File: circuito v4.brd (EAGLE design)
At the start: 93.5 x 59.5 mm, 64 parts, among them IC1 LM324N

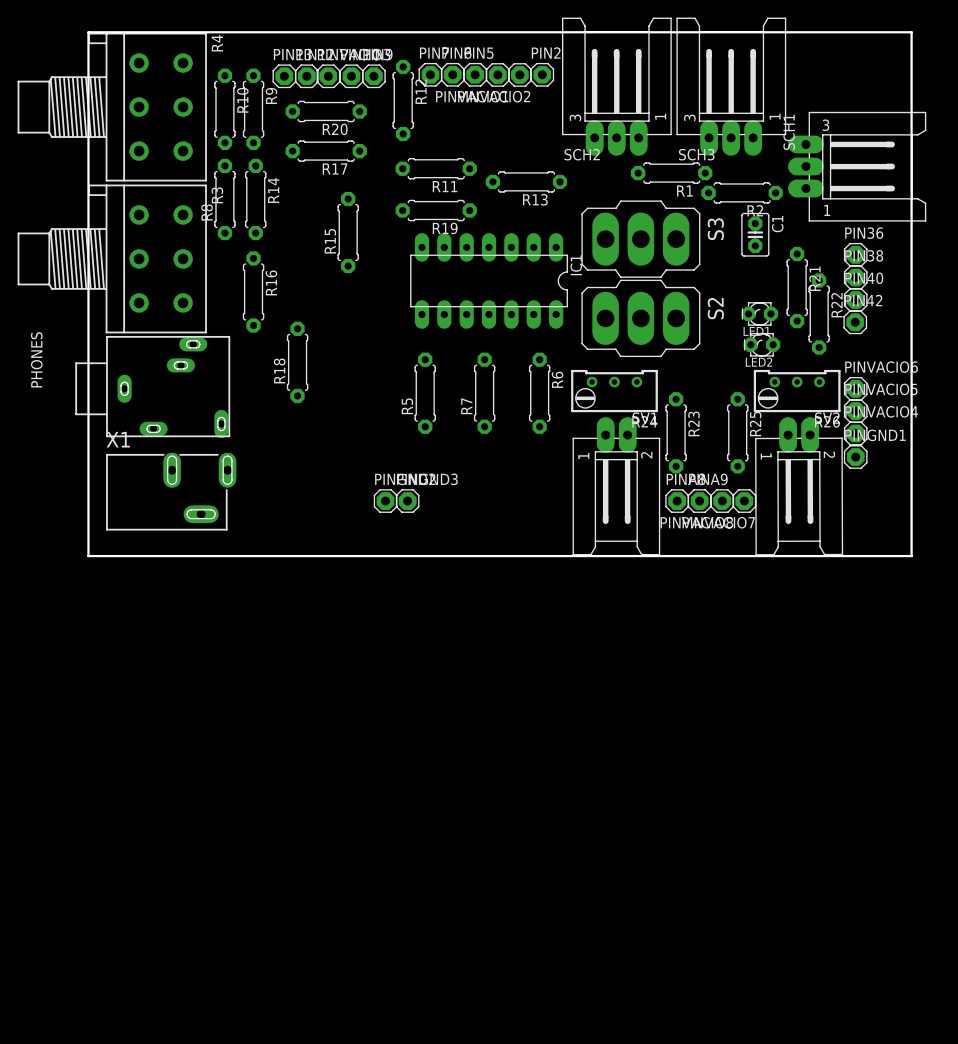
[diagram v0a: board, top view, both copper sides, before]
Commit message: board y sch con elemento ICSP del arduino incluido
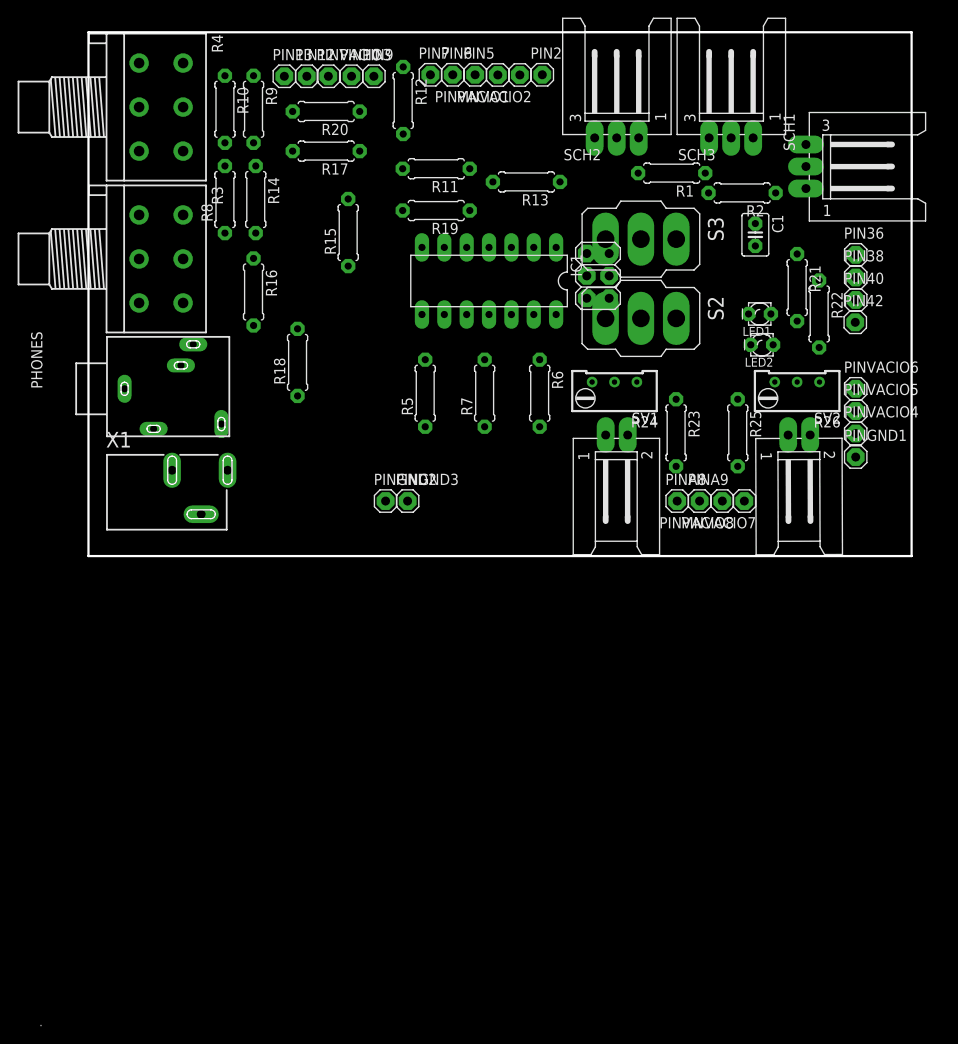
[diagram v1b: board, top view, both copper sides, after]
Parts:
- added JP19: (no value), pinhead:2X03
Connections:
- new net 5V_2: JP19.2
- new net CLK: JP19.3
- new net MISO: JP19.1
- new net MOSI: JP19.4
- new net RESET_2: JP19.5
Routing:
- added copper zone on layer 16, net N$10
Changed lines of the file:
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@@
 <grid distance="0.25" unitdist="mm" unit="mm" style="lines" multiple="1" display="yes" altdistance="0.025" altunitdist="inch" altunit="inch"/>
 <layers>
-<layer number="1" name="Top" color="4" fill="1" visible="yes" active="yes"/>
+<layer number="1" name="Top" color="4" fill="1" visible="no" active="yes"/>
 <layer number="2" name="Route2" color="1" fill="3" visible="no" active="no"/>
 <layer number="3" name="Route3" color="4" fill="3" visible="no" active="no"/>
@@
 <layer number="14" name="Route14" color="1" fill="6" visible="no" active="no"/>
 <layer number="15" name="Route15" color="4" fill="6" visible="no" active="no"/>
-<layer number="16" name="Bottom" color="1" fill="1" visible="yes" active="yes"/>
-<layer number="17" name="Pads" color="2" fill="1" visible="yes" active="yes"/>
-<layer number="18" name="Vias" color="2" fill="1" visible="yes" active="yes"/>
+<layer number="16" name="Bottom" color="1" fill="1" visible="no" active="yes"/>
+<layer number="17" name="Pads" color="2" fill="1" visible="no" active="yes"/>
+<layer number="18" name="Vias" color="2" fill="1" visible="no" active="yes"/>
 <layer number="19" name="Unrouted" color="6" fill="1" visible="yes" active="yes"/>
 <layer number="20" name="Dimension" color="15" fill="1" visible="yes" active="yes"/>
@@
 <layer number="39" name="tKeepout" color="4" fill="11" visible="yes" active="yes"/>
 <layer number="40" name="bKeepout" color="1" fill="11" visible="yes" active="yes"/>
-<layer number="41" name="tRestrict" color="4" fill="10" visible="yes" active="yes"/>
-<layer number="42" name="bRestrict" color="1" fill="10" visible="yes" active="yes"/>
+<layer number="41" name="tRestrict" color="4" fill="10" visible="no" active="yes"/>
+<layer number="42" name="bRestrict" color="1" fill="10" visible="no" active="yes"/>
 <layer number="43" name="vRestrict" color="2" fill="10" visible="no" active="yes"/>
 <layer number="44" name="Drills" color="7" fill="1" visible="no" active="yes"/>
@@
 <attribute name="VALUE" x="59.975" y="34.79" size="1.778" layer="27" ratio="10" rot="R270"/>
 </element>
+<element name="JP19" library="pinhead" package="2X03" value="" x="64.625796875" y="28.07624375" smashed="yes" rot="R90">
+<attribute name="VALUE" x="69.070796875" y="24.26624375" size="1.27" layer="27" rot="R90"/>
+</element>
 </elements>
 <signals>
@@
 <wire x1="80.5" y1="14.06" x2="84.71" y2="16.02" width="0" layer="19" extent="1-1"/>
 </signal>
+<signal name="MOSI">
+<contactref element="JP19" pad="4"/>
+</signal>
+<signal name="MISO">
+<contactref element="JP19" pad="1"/>
+</signal>
+<signal name="CLK">
+<contactref element="JP19" pad="3"/>
+</signal>
+<signal name="N$10">
+<polygon width="0" layer="16">
+<vertex x="1.353546875" y="-57.15"/>
+<vertex x="1.353546875" y="-57.004240625"/>
+<vertex x="1.3581" y="-57.004240625"/>
+</polygon>
+</signal>
+<signal name="RESET_2">
+<contactref element="JP19" pad="5"/>
+</signal>
+<signal name="5V_2">
+<contactref element="JP19" pad="2"/>
+</signal>
 </signals>

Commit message: Poligono bRestrict en ICSP
Se agregó polígono en bRestrict en ICSP.
Se corrieron elementos para que entre ese polígono.
No se agrandó la placa del lado derecho.
Se achicó del lado izquierdo para que la distancia entre el borde de la placa y el centro del pin GND sea 27mm.
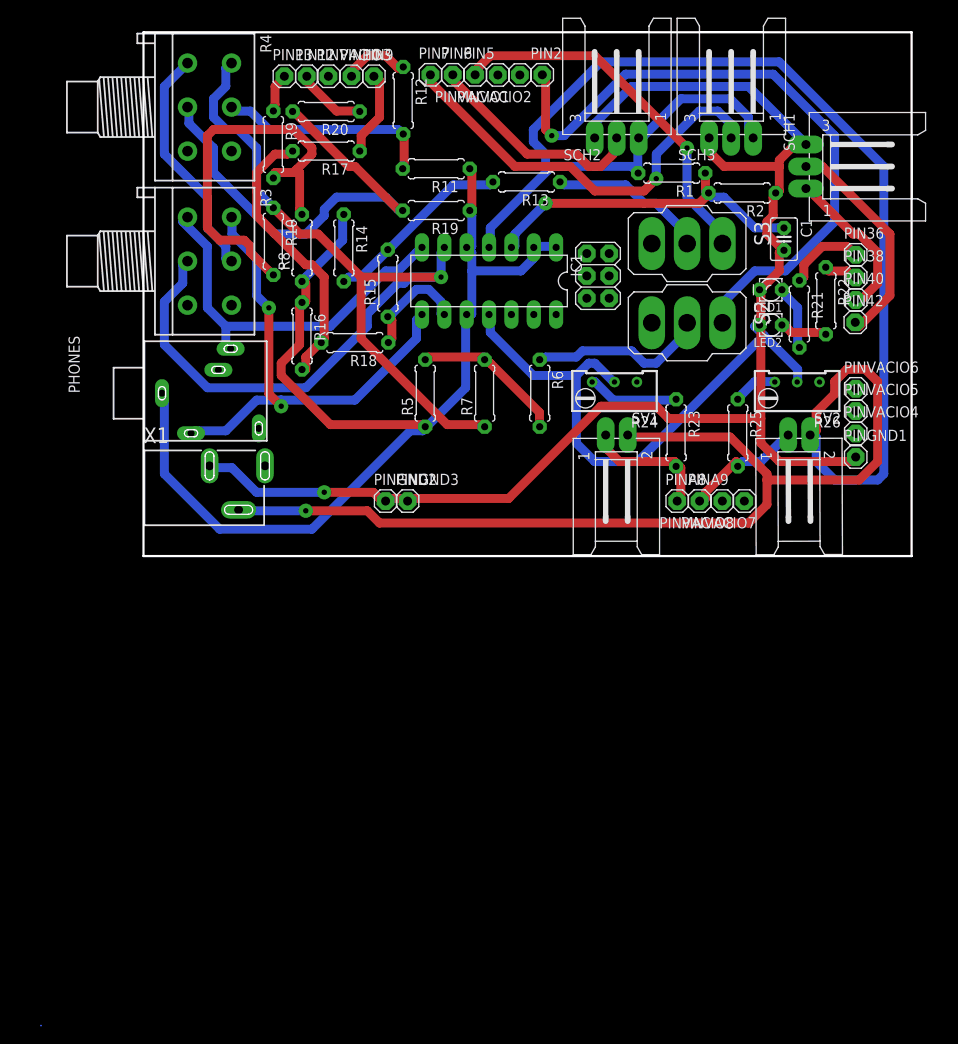
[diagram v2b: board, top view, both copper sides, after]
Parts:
- moved R10 16.0 mm to (27.8, 32.0)
- moved R14 11.4 mm to (35.8, 31.2)
- moved R8 10.3 mm to (31.0, 31.2)
- moved R16 7.43 mm to (31.0, 21.2)
- moved R15 7.30 mm to (40.8, 27.2)
- moved R18 6.88 mm to (37.0, 20.5), turned to 180 degrees
- moved R3 5.51 mm to (18.0, 29.8)
- moved R4 5.50 mm to (18.0, 47.2)
- moved S2 5.27 mm to (74.8, 22.8)
- moved S3 5.27 mm to (74.8, 31.8)
- moved R9 4.59 mm to (27.8, 43.0)
- moved PHONES 4.28 mm to (13.0, 14.8)
- moved X1 4.28 mm to (13.0, 4.00)
- moved C1 3.29 mm to (85.8, 32.2)
- moved LED1 3.02 mm to (84.2, 26.5)
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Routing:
- net VCC: track 0.00 -> 263.0 mm, vias 0 -> 1
- net GND: track 0.00 -> 225.1 mm, vias 0 -> 1
- net N$8: track 0.00 -> 131.2 mm
- net N$4: track 0.00 -> 122.1 mm, vias 0 -> 1
- net N$7: track 0.00 -> 73.8 mm, vias 0 -> 1
- net N$30: track 0.00 -> 57.5 mm, vias 0 -> 2
- net N$18: track 0.00 -> 52.9 mm
- net N$28: track 0.00 -> 47.7 mm, vias 0 -> 1
- net N$9: track 0.00 -> 45.3 mm
- net N$37: track 0.00 -> 43.4 mm
- net N$16: track 0.00 -> 42.3 mm, vias 0 -> 1
- net N$13: track 0.00 -> 39.9 mm
- net N$1: track 0.00 -> 38.5 mm, vias 0 -> 1
- net N$19: track 0.00 -> 32.3 mm
- net N$29: track 0.00 -> 25.4 mm
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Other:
- board size 93.5 x 59.5 mm -> 87.2 x 59.5 mm

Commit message: Agrego vRestrict en OpAmp y Switchs
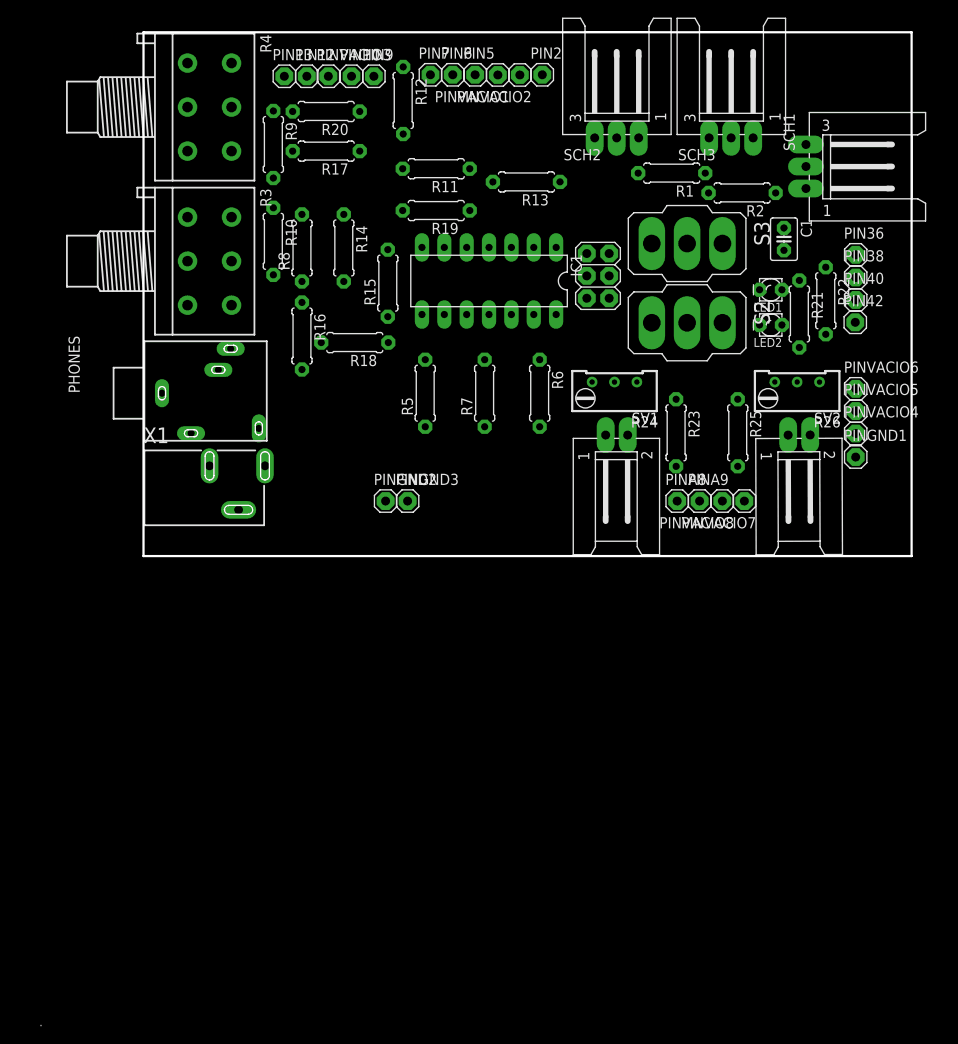
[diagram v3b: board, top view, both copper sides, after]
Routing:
- net VCC: track 263.0 -> 0.00 mm, vias 1 -> 0
- net GND: track 225.1 -> 0.00 mm, vias 1 -> 0
- net N$8: track 131.2 -> 0.00 mm
- net N$4: track 122.1 -> 0.00 mm, vias 1 -> 0
- net N$7: track 73.8 -> 0.00 mm, vias 1 -> 0
- net N$30: track 57.5 -> 0.00 mm, vias 2 -> 0
- net N$18: track 52.9 -> 0.00 mm
- net N$28: track 47.7 -> 0.00 mm, vias 1 -> 0
- net N$9: track 45.3 -> 0.00 mm
- net N$37: track 43.4 -> 0.00 mm
- net N$16: track 42.3 -> 0.00 mm, vias 1 -> 0
- net N$13: track 39.9 -> 0.00 mm
- net N$1: track 38.5 -> 0.00 mm, vias 1 -> 0
- net N$19: track 32.3 -> 0.00 mm
- net N$29: track 25.4 -> 0.00 mm
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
